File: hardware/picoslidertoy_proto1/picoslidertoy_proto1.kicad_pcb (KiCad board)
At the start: 2 copper layers, 165.1 x 76.2 mm, 50 parts, among them SW1 Capacitive Button, SW2 Capacitive Button, SW3 Capacitive Button, SW4 Capacitive Button, SW5 Capacitive Button, SW6 Capacitive Button, SW7 Capacitive Button, SW8 Capacitive Button, SW9 Capacitive Button, U1 Pico

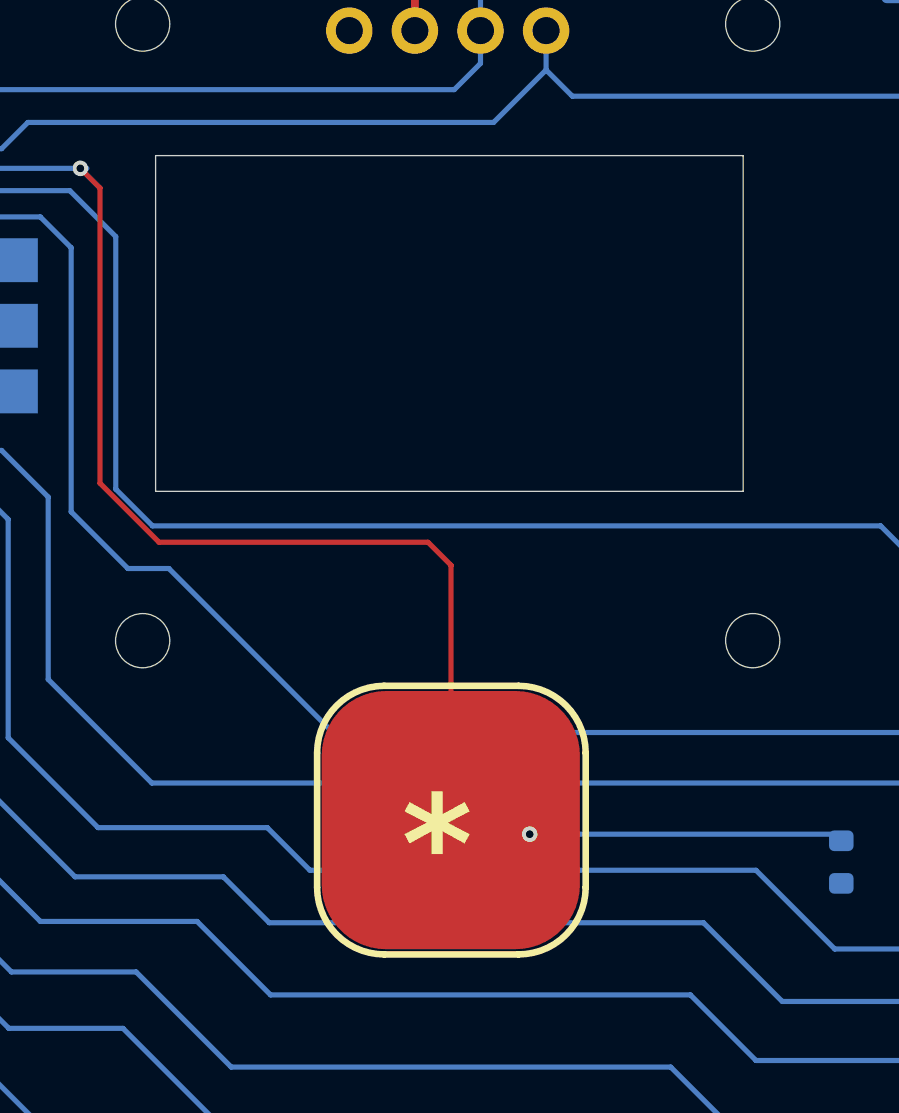
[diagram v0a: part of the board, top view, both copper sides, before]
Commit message: circuitpython slider_test as in picoslider prototype demo video, save proto1 pcb as own kicad project
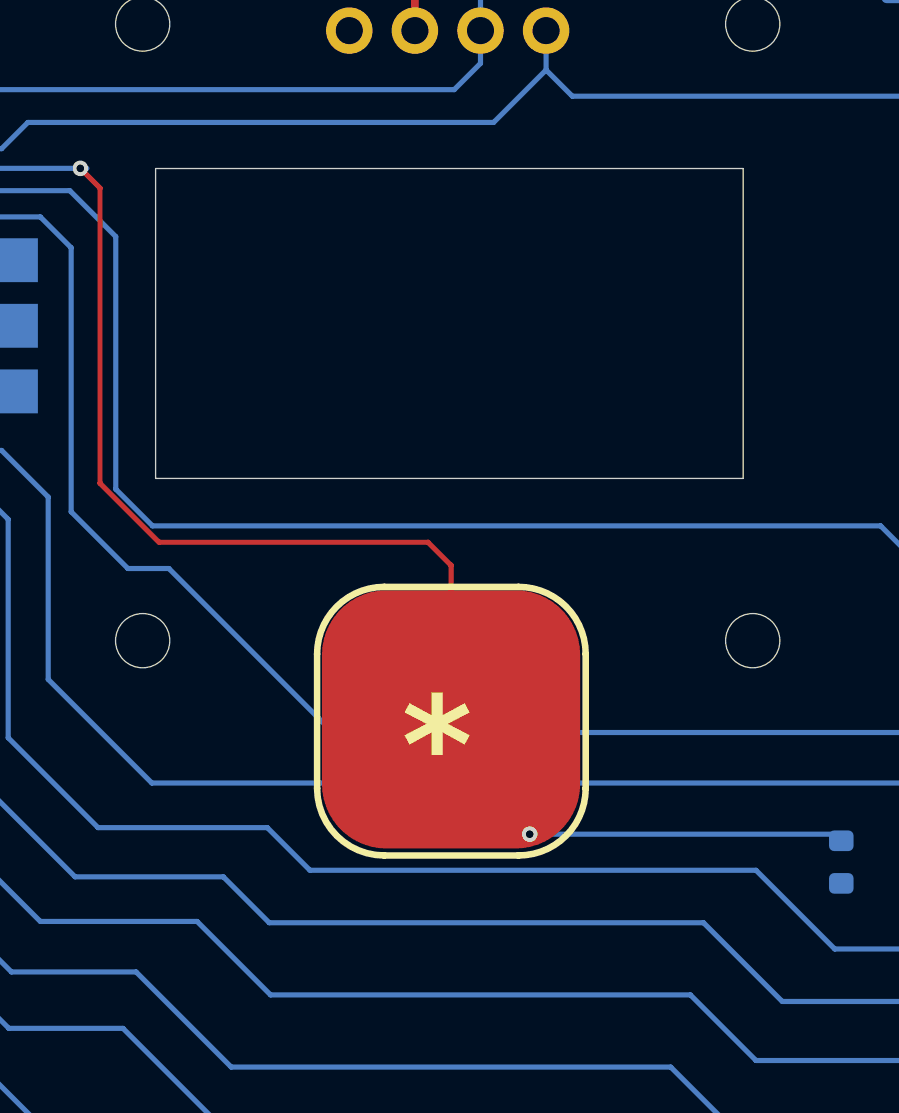
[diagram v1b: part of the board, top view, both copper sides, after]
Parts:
- moved SW9 3.90 mm to (94.1, 63.5)
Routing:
- net /TPAD9: track 63.4 -> 59.5 mm
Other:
- outline, holes or cut-outs redrawn
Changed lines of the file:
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@@
 	(footprint "SparkFun-Switch:Pad-CapacitiveTouch"
 		(layer "F.Cu")
-		(at 94.1 67.4)
+		(at 94.11 63.5)
 		(descr "<h3>Conductive Button</h3>\n<p>Used with rubber key pads on the <a href=\"https://www.sparkfun.com/products/retired/8602\">Nordic Key FOB</a>. This one was designed and proven to work with the <a href=\"https://www.sparkfun.com/products/retired/9377\">PolyCase Key FOB enclosures</a>.</p>")
 		(property "Reference" "SW9"
@@
 		(tags "resistor")
 		(property "Reference" "R24"
-			(at 0 1.43 -90)
+			(at 0 1.43 270)
 			(layer "B.SilkS")
 			(effects
@@
 		)
 		(property "Value" "1M"
-			(at 0 -1.43 -90)
+			(at 0 -1.43 270)
 			(layer "B.Fab")
 			(effects
@@
 		)
 		(fp_text user "${REFERENCE}"
-			(at 0 0 -90)
+			(at 0 0 270)
 			(layer "B.Fab")
 			(effects
@@
 	)
 	(gr_line
-		(start 91.5232 62.2)
-		(end 96.7232 62.2)
+		(start 91.5232 58.3692)
+		(end 96.7232 58.3692)
 		(stroke
 			(width 0.254)
@@
 	)
 	(gr_line
-		(start 88.923201 69.999999)
-		(end 88.9232 64.8)
+		(start 88.923201 66.169199)
+		(end 88.9232 60.9692)
 		(stroke
 			(width 0.254)
@@
 	)
 	(gr_arc
-		(start 91.523201 72.599999)
-		(mid 89.684723 71.838477)
-		(end 88.923201 69.999999)
+		(start 91.523201 68.769199)
+		(mid 89.684724 68.007676)
+		(end 88.923201 66.169199)
 		(stroke
 			(width 0.254)
@@
 	)
 	(gr_arc
-		(start 88.9232 64.8)
-		(mid 89.684722 62.961522)
-		(end 91.5232 62.2)
+		(start 88.9232 60.9692)
+		(mid 89.684722 59.130722)
+		(end 91.5232 58.3692)
 		(stroke
 			(width 0.254)
@@
 	)
 	(gr_arc
-		(start 96.7232 62.2)
-		(mid 98.561678 62.961522)
-		(end 99.3232 64.8)
+		(start 96.7232 58.3692)
+		(mid 98.561679 59.130721)
+		(end 99.3232 60.9692)
 		(stroke
 			(width 0.254)
@@
 	)
 	(gr_line
-		(start 96.723199 72.599999)
-		(end 91.523201 72.599999)
+		(start 96.723199 68.769199)
+		(end 91.523201 68.769199)
 		(stroke
 			(width 0.254)
@@
 	)
 	(gr_arc
-		(start 99.323199 69.999999)
-		(mid 98.561677 71.838477)
-		(end 96.723199 72.599999)
+		(start 99.323199 66.169199)
+		(mid 98.561677 68.007677)
+		(end 96.723199 68.769199)
 		(stroke
 			(width 0.254)
@@
 	)
 	(gr_line
-		(start 99.323199 70)
-		(end 99.3232 64.800001)
+		(start 99.323199 66.1692)
+		(end 99.3232 60.969201)
 		(stroke
 			(width 0.254)
@@
 	)
 	(gr_rect
-		(start 82.67 41.67)
-		(end 105.42 54.67)
+		(start 82.67 42.17)
+		(end 105.42 54.17)
 		(stroke
 			(width 0.05)
@@
 	)
 	(gr_text "*"
-		(at 92.202 70.6328 0)
+		(at 92.202 66.802 0)
 		(layer "F.SilkS")
 		(effects
@@
 	)
 	(segment
-		(start 80.518 42.926)
-		(end 80.518 54.356)
+		(start 94.107 57.531)
+		(end 94.11 57.528)
 		(width 0.2)
 		(layer "F.Cu")
@@
 	)
 	(segment
-		(start 94.11 67.39)
-		(end 94.1 67.4)
+		(start 79.756 42.164)
+		(end 80.518 42.926)
 		(width 0.2)
 		(layer "F.Cu")
@@
 	)
 	(segment
-		(start 79.756 42.164)
-		(end 80.518 42.926)
-		(width 0.2)
-		(layer "F.Cu")
-		(net 36)
-	)
-	(segment
 		(start 93.218 56.642)
 		(end 94.107 57.531)
@@
 	)
 	(segment
-		(start 94.107 57.531)
-		(end 94.11 57.528)
+		(start 94.11 57.528)
+		(end 94.11 63.5)
 		(width 0.2)
 		(layer "F.Cu")
@@
 	)
 	(segment
-		(start 94.11 57.528)
-		(end 94.11 67.39)
+		(start 80.518 42.926)
+		(end 80.518 54.356)
 		(width 0.2)
 		(layer "F.Cu")
